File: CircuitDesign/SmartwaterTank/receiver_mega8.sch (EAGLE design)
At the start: 13 parts, among them T1 2N2222

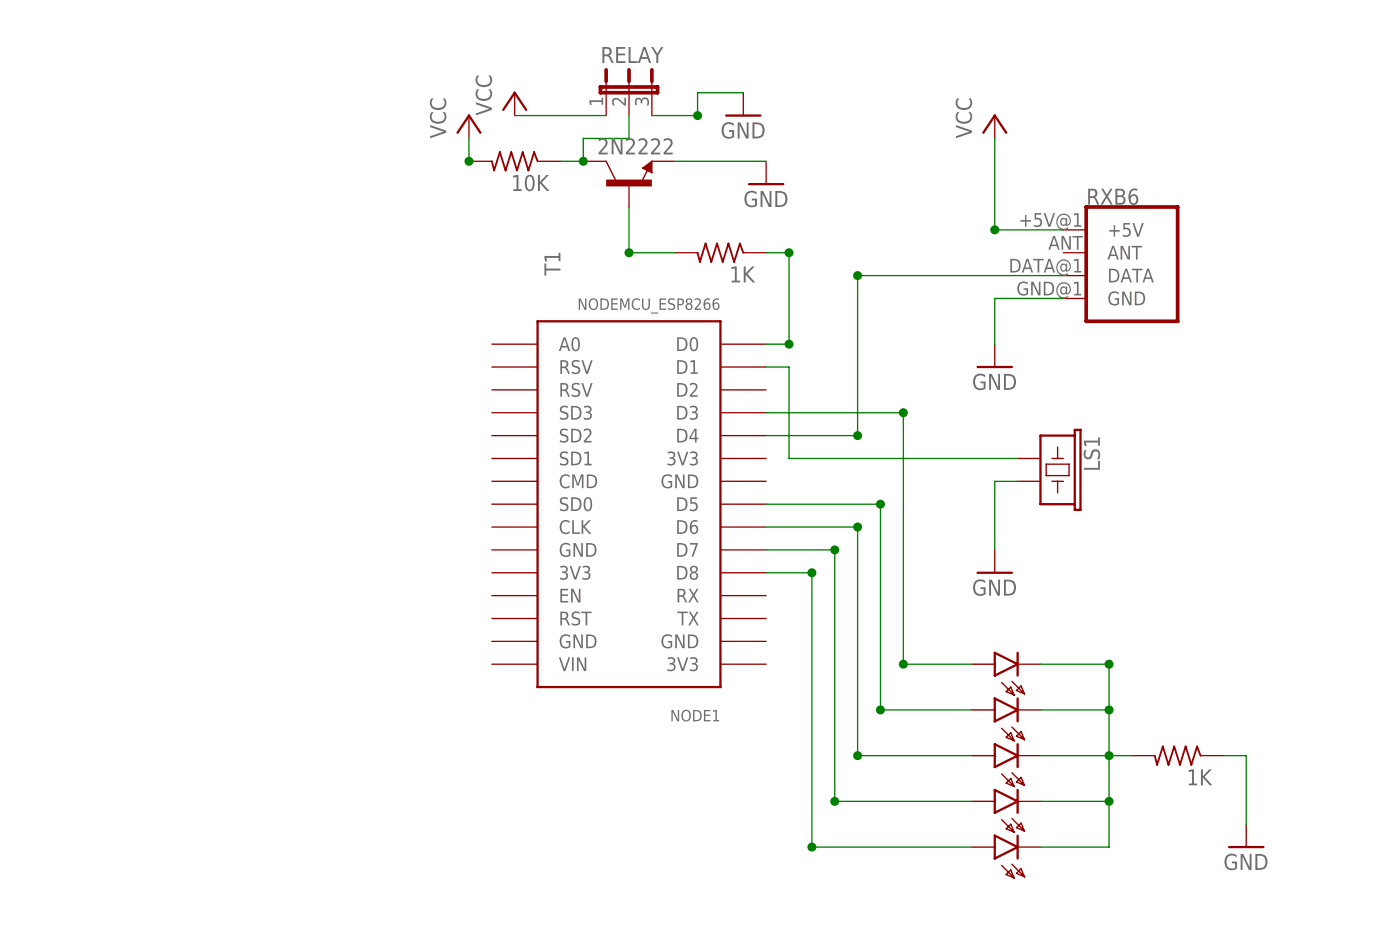
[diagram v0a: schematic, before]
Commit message: Issue #6: add receiver schema for atmega8
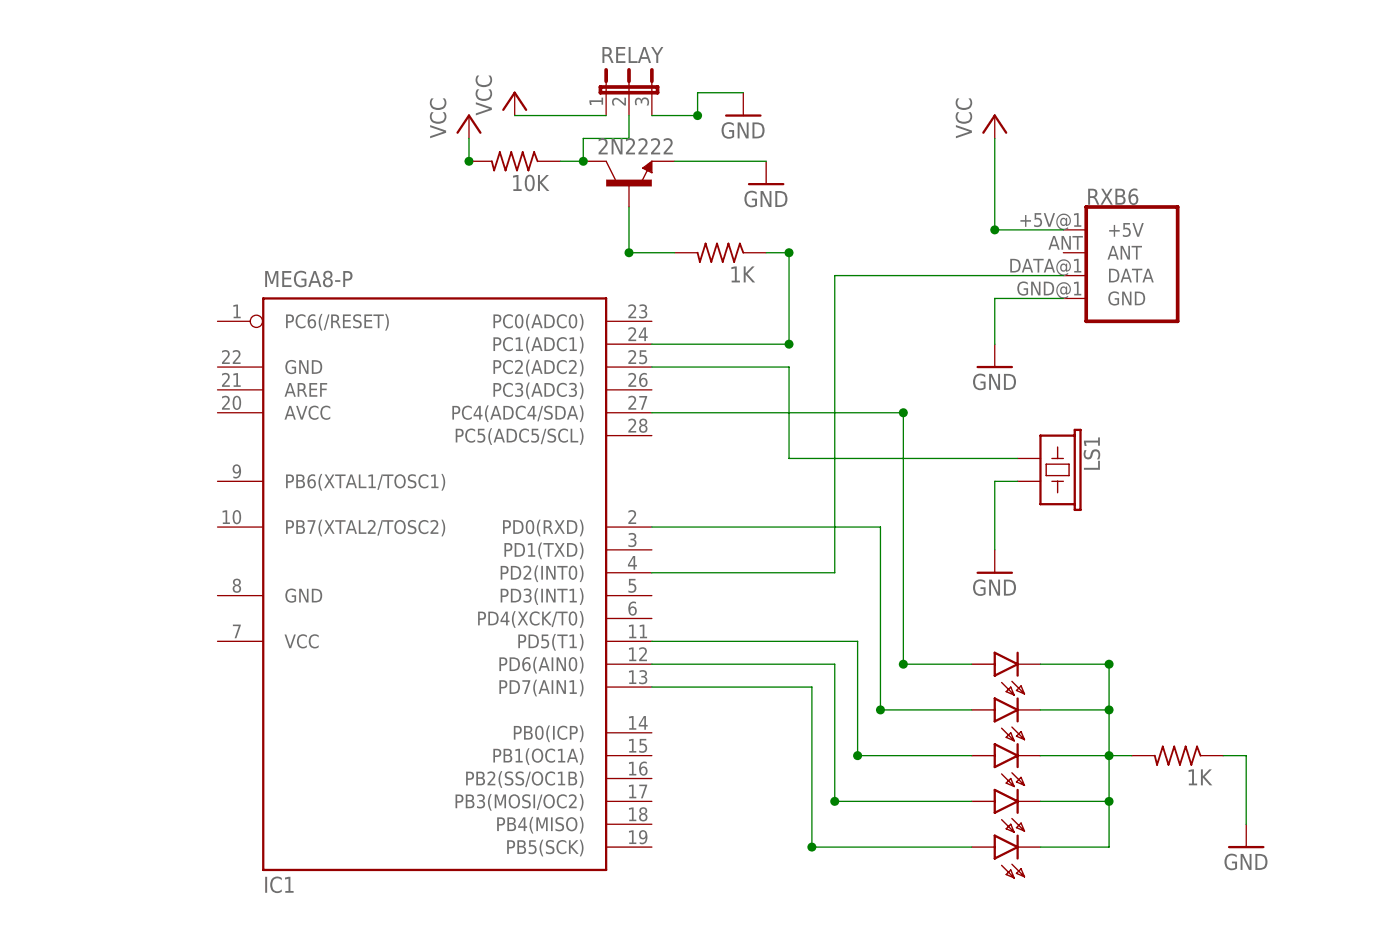
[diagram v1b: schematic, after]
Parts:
- removed NODE1: NODEMCU_ESP8266, nodemcu_esp8266:NODEMCU_ESP8266
- added IC1: MEGA8-P, atmel:MEGA8-P
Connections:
- net N$10: now also IC1.PD7(AIN1); no longer NODE1.D8
- net N$11: now also IC1.PD6(AIN0); no longer NODE1.D7
- net N$12: now also IC1.PD5(T1); no longer NODE1.D6
- net N$13: now also IC1.PD0(RXD); no longer NODE1.D5
- net N$15: now also IC1.PC4(ADC4/SDA); no longer NODE1.D3
- net N$2: now also IC1.PC1(ADC1); no longer NODE1.D0
- net N$4: now also IC1.PD2(INT0); no longer NODE1.D4
- net N$5: now also IC1.PC2(ADC2); no longer NODE1.D1
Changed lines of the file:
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@@
 <part name="GND5" library="supply1" library_urn="urn:adsk.eagle:library:371" deviceset="GND" device=""/>
 <part name="R1" library="rcl" library_urn="urn:adsk.eagle:library:334" deviceset="R-US_" device="0207/12" package3d_urn="urn:adsk.eagle:package:23489/1" value="1K"/>
-<part name="NODE1" library="nodemcu_esp8266" deviceset="NODEMCU_ESP8266" device=""/>
 <part name="T1" library="transistor" library_urn="urn:adsk.eagle:library:402" deviceset="*-NPN-" device="TO92-CBE" package3d_urn="urn:adsk.eagle:package:29921/2" technology="2N4124" value="2N2222"/>
 <part name="P+2" library="supply1" library_urn="urn:adsk.eagle:library:371" deviceset="VCC" device=""/>
@@
 <part name="R2" library="rcl" library_urn="urn:adsk.eagle:library:334" deviceset="R-US_" device="0207/12" package3d_urn="urn:adsk.eagle:package:23489/1" value="1K"/>
 <part name="LS1" library="SparkFun-Electromechanical" deviceset="BUZZER" device="-PTH_KIT"/>
+<part name="IC1" library="atmel" library_urn="urn:adsk.eagle:library:105" deviceset="MEGA8-P" device="" package3d_urn="urn:adsk.eagle:package:4320/1"/>
 </parts>
 <sheets>
@@
 <attribute name="VALUE" x="59.69" y="187.198" size="1.778" layer="96" rot="MR0"/>
 </instance>
-<instance part="NODE1" gate="G$1" x="45.72" y="157.48" smashed="yes" rot="R180">
-<attribute name="VALUE" x="55.88" y="185.42" size="1.27" layer="96" rot="R180"/>
-<attribute name="NAME" x="55.88" y="139.7" size="1.27" layer="95" rot="R180"/>
-</instance>
 <instance part="T1" gate="G$1" x="45.72" y="198.12" smashed="yes" rot="R90">
-<attribute name="NAME" x="38.1" y="187.96" size="1.778" layer="95" rot="R90"/>
 <attribute name="VALUE" x="50.8" y="203.2" size="1.778" layer="96" rot="R180"/>
 </instance>
@@
 <instance part="LS1" gate="G$1" x="91.44" y="167.64" smashed="yes" rot="R270">
 <attribute name="NAME" x="96.266" y="170.18" size="1.778" layer="95" font="vector" rot="R270"/>
+</instance>
+<instance part="IC1" gate="G$1" x="22.86" y="154.94" smashed="yes">
+<attribute name="NAME" x="5.08" y="119.38" size="1.778" layer="95"/>
+<attribute name="VALUE" x="5.08" y="186.69" size="1.778" layer="96"/>
 </instance>
 </instances>
@@
 <pinref part="D6" gate="A" pin="A"/>
 <wire x1="83.82" y1="124.46" x2="66.04" y2="124.46" width="0.1524" layer="91"/>
-<wire x1="66.04" y1="124.46" x2="66.04" y2="154.94" width="0.1524" layer="91"/>
-<pinref part="NODE1" gate="G$1" pin="D8"/>
-<wire x1="66.04" y1="154.94" x2="60.96" y2="154.94" width="0.1524" layer="91"/>
+<wire x1="66.04" y1="124.46" x2="66.04" y2="142.24" width="0.1524" layer="91"/>
 <junction x="66.04" y="124.46"/>
-<junction x="66.04" y="154.94"/>
+<pinref part="IC1" gate="G$1" pin="PD7(AIN1)"/>
+<wire x1="48.26" y1="142.24" x2="66.04" y2="142.24" width="0.1524" layer="91"/>
 </segment>
 </net>
@@
 <pinref part="D5" gate="A" pin="A"/>
 <wire x1="83.82" y1="129.54" x2="68.58" y2="129.54" width="0.1524" layer="91"/>
-<wire x1="68.58" y1="157.48" x2="68.58" y2="129.54" width="0.1524" layer="91"/>
-<pinref part="NODE1" gate="G$1" pin="D7"/>
-<wire x1="68.58" y1="157.48" x2="60.96" y2="157.48" width="0.1524" layer="91"/>
+<wire x1="68.58" y1="144.78" x2="68.58" y2="129.54" width="0.1524" layer="91"/>
 <junction x="68.58" y="129.54"/>
-<junction x="68.58" y="157.48"/>
+<pinref part="IC1" gate="G$1" pin="PD6(AIN0)"/>
+<wire x1="48.26" y1="144.78" x2="68.58" y2="144.78" width="0.1524" layer="91"/>
 </segment>
 </net>
@@
 <pinref part="D4" gate="A" pin="A"/>
 <wire x1="83.82" y1="134.62" x2="71.12" y2="134.62" width="0.1524" layer="91"/>
-<wire x1="71.12" y1="134.62" x2="71.12" y2="160.02" width="0.1524" layer="91"/>
-<pinref part="NODE1" gate="G$1" pin="D6"/>
-<wire x1="71.12" y1="160.02" x2="60.96" y2="160.02" width="0.1524" layer="91"/>
+<wire x1="71.12" y1="134.62" x2="71.12" y2="147.32" width="0.1524" layer="91"/>
 <junction x="71.12" y="134.62"/>
-<junction x="71.12" y="160.02"/>
+<pinref part="IC1" gate="G$1" pin="PD5(T1)"/>
+<wire x1="48.26" y1="147.32" x2="71.12" y2="147.32" width="0.1524" layer="91"/>
 </segment>
 </net>
@@
 <pinref part="D3" gate="A" pin="A"/>
 <wire x1="83.82" y1="139.7" x2="73.66" y2="139.7" width="0.1524" layer="91"/>
-<wire x1="73.66" y1="139.7" x2="73.66" y2="162.56" width="0.1524" layer="91"/>
-<pinref part="NODE1" gate="G$1" pin="D5"/>
-<wire x1="73.66" y1="162.56" x2="60.96" y2="162.56" width="0.1524" layer="91"/>
+<wire x1="73.66" y1="139.7" x2="73.66" y2="160.02" width="0.1524" layer="91"/>
 <junction x="73.66" y="139.7"/>
-<junction x="73.66" y="162.56"/>
+<pinref part="IC1" gate="G$1" pin="PD0(RXD)"/>
+<wire x1="48.26" y1="160.02" x2="73.66" y2="160.02" width="0.1524" layer="91"/>
 </segment>
 </net>
@@
 <segment>
 <pinref part="R1" gate="G$1" pin="1"/>
-<pinref part="NODE1" gate="G$1" pin="D0"/>
-<wire x1="60.96" y1="180.34" x2="63.5" y2="180.34" width="0.1524" layer="91"/>
 <wire x1="63.5" y1="180.34" x2="63.5" y2="190.5" width="0.1524" layer="91"/>
 <wire x1="63.5" y1="190.5" x2="60.96" y2="190.5" width="0.1524" layer="91"/>
 <junction x="63.5" y="190.5"/>
 <junction x="63.5" y="180.34"/>
+<pinref part="IC1" gate="G$1" pin="PC1(ADC1)"/>
+<wire x1="63.5" y1="180.34" x2="48.26" y2="180.34" width="0.1524" layer="91"/>
 </segment>
 </net>
@@
 <segment>
 <pinref part="RXB6" gate="G$1" pin="DATA"/>
-<wire x1="93.98" y1="187.96" x2="71.12" y2="187.96" width="0.1524" layer="91"/>
-<junction x="71.12" y="187.96"/>
-<pinref part="NODE1" gate="G$1" pin="D4"/>
-<wire x1="60.96" y1="170.18" x2="71.12" y2="170.18" width="0.1524" layer="91"/>
-<junction x="71.12" y="170.18"/>
-<wire x1="71.12" y1="187.96" x2="71.12" y2="170.18" width="0.1524" layer="91"/>
+<wire x1="93.98" y1="187.96" x2="68.58" y2="187.96" width="0.1524" layer="91"/>
+<wire x1="68.58" y1="187.96" x2="68.58" y2="154.94" width="0.1524" layer="91"/>
+<pinref part="IC1" gate="G$1" pin="PD2(INT0)"/>
+<wire x1="68.58" y1="154.94" x2="48.26" y2="154.94" width="0.1524" layer="91"/>
 </segment>
 </net>
@@
 <segment>
 <wire x1="63.5" y1="167.64" x2="63.5" y2="177.8" width="0.1524" layer="91"/>
-<pinref part="NODE1" gate="G$1" pin="D1"/>
-<wire x1="63.5" y1="177.8" x2="60.96" y2="177.8" width="0.1524" layer="91"/>
 <pinref part="LS1" gate="G$1" pin="1"/>
 <wire x1="88.9" y1="167.64" x2="63.5" y2="167.64" width="0.1524" layer="91"/>
+<pinref part="IC1" gate="G$1" pin="PC2(ADC2)"/>
+<wire x1="63.5" y1="177.8" x2="48.26" y2="177.8" width="0.1524" layer="91"/>
 </segment>
 </net>
@@
 <wire x1="83.82" y1="144.78" x2="76.2" y2="144.78" width="0.1524" layer="91"/>
 <wire x1="76.2" y1="172.72" x2="76.2" y2="144.78" width="0.1524" layer="91"/>
-<pinref part="NODE1" gate="G$1" pin="D3"/>
-<wire x1="76.2" y1="172.72" x2="60.96" y2="172.72" width="0.1524" layer="91"/>
+<wire x1="76.2" y1="172.72" x2="48.26" y2="172.72" width="0.1524" layer="91"/>
 <junction x="76.2" y="144.78"/>
 <junction x="76.2" y="172.72"/>
-</segment>
-</net>
+<pinref part="IC1" gate="G$1" pin="PC4(ADC4/SDA)"/>
+</segment>
+</net>

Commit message: Issue #6: update receiver board for vero board
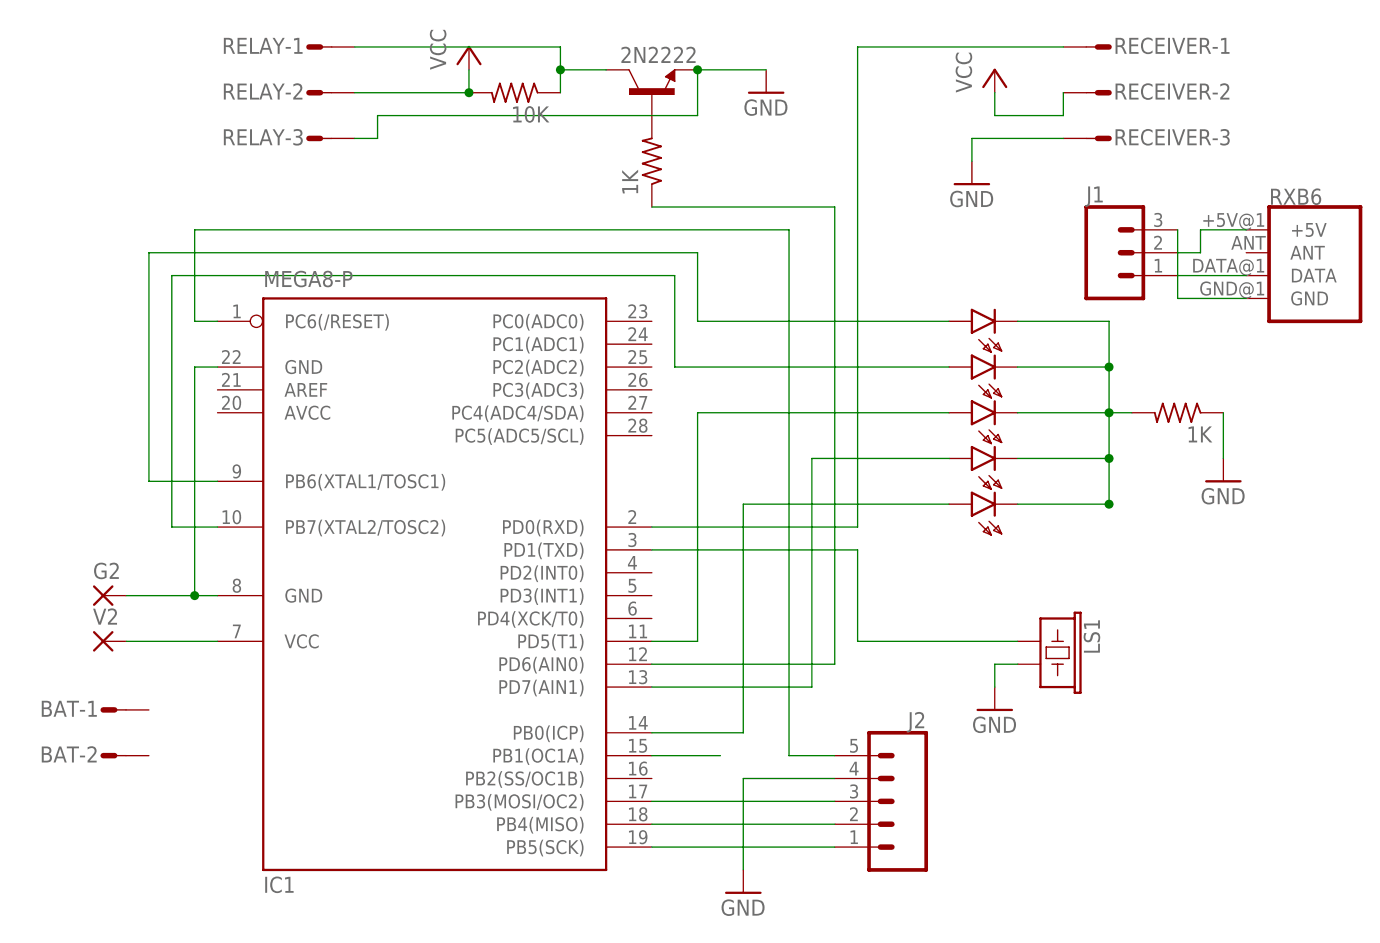
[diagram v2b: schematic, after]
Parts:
- added BAT: (no value), con-amp-mt:S02P
- added G2, V2: (no value), wirepad:1,6/0,8
- added J1: (no value), SparkFun-Connectors:CONN_03
- added J2: (no value), SparkFun-Connectors:CONN_05
- added RECEIVER: (no value), con-amp-mt:S03P
- RELAY: device jumper:JP2E -> con-amp-mt:S03P
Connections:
- new net N$14: J1.2, RXB6.+5V
- new net N$16: R5.1, RELAY-1.S, T1.C
- new net N$17: IC1.PB5(SCK), J2.1
- new net N$18: IC1.PB4(MISO), J2.2
- new net N$19: IC1.PB3(MOSI/OC2), J2.3
- new net N$20: IC1.PB1(OC1A)
- new net N$22: IC1.PC6(/RESET), J2.5
- new net N$7: G2.P, IC1.GND, IC1.GND@1
- new net N$8: IC1.VCC@1, V2.P
- new net N$9: J1.3, RXB6.GND
- net GND: now also J2.4, RECEIVER-3.S, RELAY-3.S; no longer RELAY.3, RXB6.GND
- net N$10: now also IC1.PB6(XTAL1/TOSC1); no longer IC1.PD7(AIN1)
- net N$11: now also IC1.PB7(XTAL2/TOSC2); no longer IC1.PD6(AIN0)
- net N$13: now also IC1.PD7(AIN1); no longer IC1.PD0(RXD)
- net N$15: now also IC1.PB0(ICP); no longer IC1.PC4(ADC4/SDA)
- net N$2: now also IC1.PD6(AIN0); no longer IC1.PC1(ADC1)
- net N$3: now also J1.1, RXB6.DATA; no longer R5.1, RELAY.2, T1.C
- net N$4: now also IC1.PD0(RXD), RECEIVER-1.S; no longer IC1.PD2(INT0), RXB6.DATA
- net N$5: now also IC1.PD1(TXD); no longer IC1.PC2(ADC2)
- net VCC: now also RECEIVER-2.S, RELAY-2.S; no longer RELAY.1, RXB6.+5V
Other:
- moved on the sheet: LS1, RXB6
